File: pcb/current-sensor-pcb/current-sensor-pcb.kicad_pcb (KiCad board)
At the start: 2 copper layers, 35 x 45.2 mm, 17 parts, among them U1 TLI4971A050T5UE0001XUMA1

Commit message: Current sensor progress
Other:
- board size 35 x 45.2 mm -> 35 x 43.5 mm

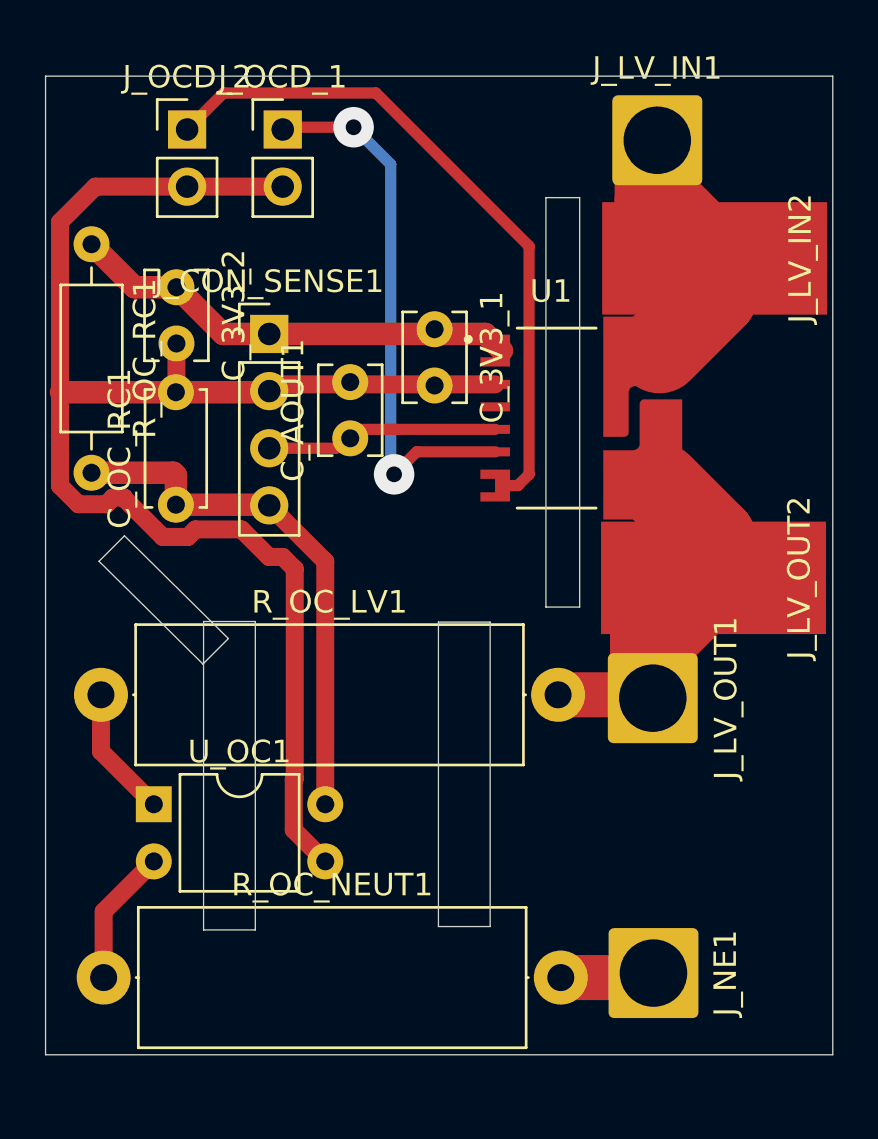
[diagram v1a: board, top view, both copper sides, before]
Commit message: Fixes to relief, JST connectors for SMT board
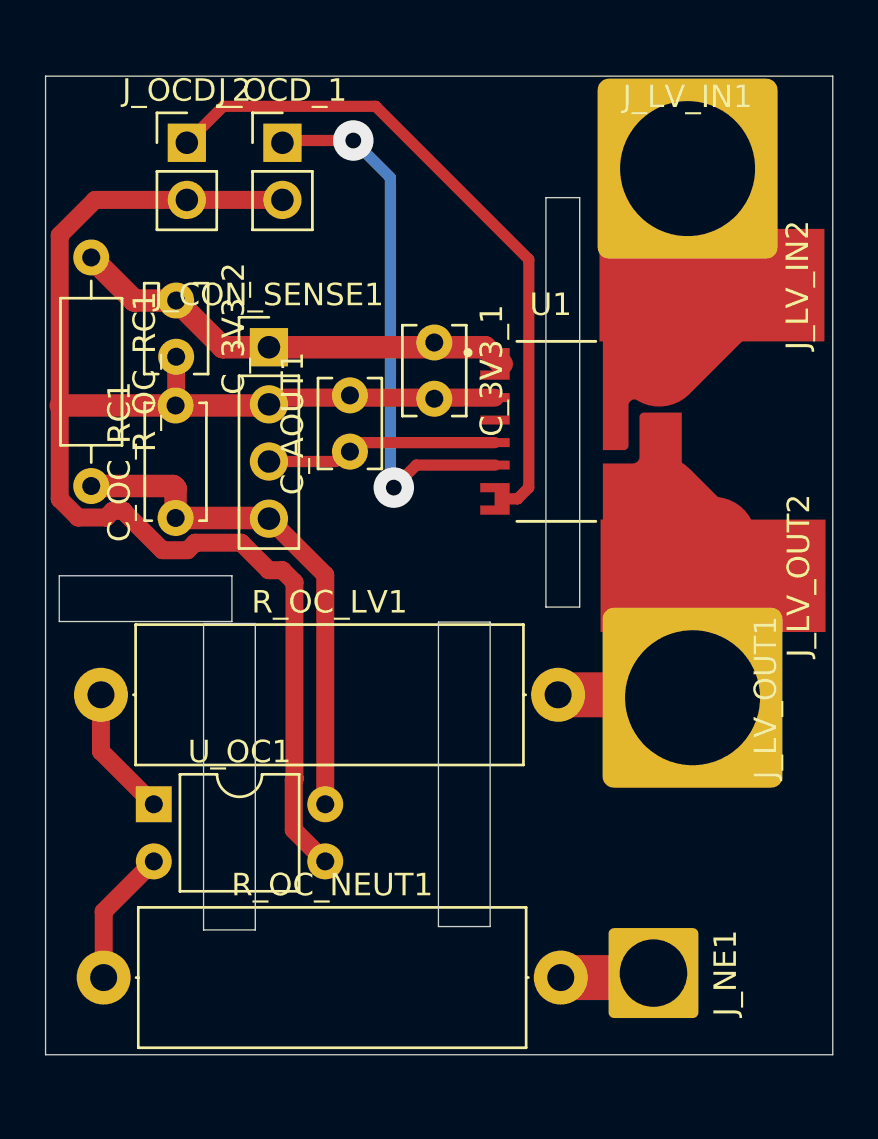
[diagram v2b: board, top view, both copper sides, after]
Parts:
- moved J_LV_IN1 1.84 mm to (28.7, 3.96)
- moved J_LV_OUT1 1.77 mm to (28.9, 27.5)
- moved J_LV_IN2 1.20 mm to (29.7, 9.14)
- moved C_3V3_1 0.59 mm to (17.4, 11.7)
- moved C_3V3_2 0.59 mm to (5.92, 9.82)
- moved C_AOUT1 0.59 mm to (13.6, 16.5)
- moved C_OC_RC1 0.59 mm to (5.89, 19.5)
- moved J_CON_SENSE1 0.59 mm to (10.0, 11.9)
- moved J_OCD_1 0.59 mm to (10.6, 2.81)
- moved J_OCD_2 0.59 mm to (6.39, 2.81)
- moved R_OC_RC1 0.59 mm to (2.14, 7.91)
- moved U1 0.59 mm to (23.9, 15.6)
- moved J_LV_OUT2 0.09 mm to (29.8, 22.1)
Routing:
- net Net-(J_CON_SENSE1-Pin_4): track 23.6 -> 23.0 mm
- net GND: track 70.0 -> 69.4 mm
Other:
- outline, holes or cut-outs redrawn

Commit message: Final changes pre manufacture
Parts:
- added J_NE2: Conn_01x01_Socket, Connector_Wire:SolderWire-2.5sqmm_1x01_D2.4mm_OD3.6mm, F.Cu at (31.2, 39.7)
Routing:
- net Net-(J_NE1-Pin_1): track 4.20 -> 8.24 mm
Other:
- board text added: "current-sensor V1 2025-05-20"
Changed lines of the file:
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@@
 	(footprint "Connector_Wire:SolderWire-2.5sqmm_1x01_D2.4mm_OD3.6mm"
 		(layer "F.Cu")
+		(at 31.1714 39.7166)
+		(descr "Soldered wire connection, for a single 2.5 mm² wire, basic insulation, conductor diameter 2.4mm, outer diameter 3.6mm, size source Multi-Contact FLEXI-E 2.5 (https://ec.staubli.com/AcroFiles/Catalogues/TM_Cab-Main-11014119_(en)_hi.pdf), bend radius 3 times outer diameter, generated with kicad-footprint-generator")
+		(tags "connector wire 2.5sqmm")
+		(property "Reference" "J_NE2"
+			(at 0 -3.2 0)
+			(layer "F.SilkS")
+			(effects
+				(font
+					(size 1 1)
+					(thickness 0.15)
+				)
+			)
+		)
+		(property "Value" "Conn_01x01_Socket"
+			(at 0 3.2 0)
+			(layer "F.Fab")
+			(effects
+				(font
+					(size 1 1)
+					(thickness 0.15)
+				)
+			)
+		)
+		(property "Footprint" "Connector_Wire:SolderWire-2.5sqmm_1x01_D2.4mm_OD3.6mm"
+			(at 0 0 0)
+			(unlocked yes)
+			(layer "F.Fab")
+			(hide yes)
+			(effects
+				(font
+					(size 1.27 1.27)
+					(thickness 0.15)
+				)
+			)
+		)
+		(property "Datasheet" ""
+			(at 0 0 0)
+			(unlocked yes)
+			(layer "F.Fab")
+			(hide yes)
+			(effects
+				(font
+					(size 1.27 1.27)
+					(thickness 0.15)
+				)
+			)
+		)
+		(property "Description" "Generic connector, single row, 01x01, script generated"
+			(at 0 0 0)
+			(unlocked yes)
+			(layer "F.Fab")
+			(hide yes)
+			(effects
+				(font
+					(size 1.27 1.27)
+					(thickness 0.15)
+				)
+			)
+		)
+		(property ki_fp_filters "Connector*:*_1x??_*")
+		(sheetname "Root")
+		(sheetfile "current-sensor-pcb.kicad_sch")
+		(attr exclude_from_pos_files)
+		(fp_line
+			(start -2.55 -2.5)
+			(end -2.55 2.5)
+			(stroke
+				(width 0.05)
+				(type solid)
+			)
+			(layer "F.CrtYd")
+		)
+		(fp_line
+			(start -2.55 2.5)
+			(end 2.55 2.5)
+			(stroke
+				(width 0.05)
+				(type solid)
+			)
+			(layer "F.CrtYd")
+		)
+		(fp_line
+			(start 2.55 -2.5)
+			(end -2.55 -2.5)
+			(stroke
+				(width 0.05)
+				(type solid)
+			)
+			(layer "F.CrtYd")
+		)
+		(fp_line
+			(start 2.55 2.5)
+			(end 2.55 -2.5)
+			(stroke
+				(width 0.05)
+				(type solid)
+			)
+			(layer "F.CrtYd")
+		)
+		(fp_circle
+			(center 0 0)
+			(end 1.8 0)
+			(stroke
+				(width 0.1)
+				(type solid)
+			)
+			(fill none)
+			(layer "F.Fab")
+		)
+		(fp_text user "${REFERENCE}"
+			(at 0 0 0)
+			(layer "F.Fab")
+			(effects
+				(font
+					(size 0.9 0.9)
+					(thickness 0.14)
+				)
+			)
+		)
+		(pad "1" thru_hole roundrect
+			(at 0 0)
+			(size 4 4)
+			(drill 3)
+			(layers "*.Cu" "*.Mask" "In1.Cu" "In2.Cu" "In3.Cu" "In4.Cu" "In5.Cu" "In6.Cu"
+				"In7.Cu" "In8.Cu" "In9.Cu" "In10.Cu" "In11.Cu" "In12.Cu" "In13.Cu" "In14.Cu"
+				"In15.Cu" "In16.Cu" "In17.Cu" "In18.Cu" "In19.Cu" "In20.Cu" "In21.Cu"
+				"In22.Cu" "In23.Cu" "In24.Cu" "In25.Cu" "In26.Cu" "In27.Cu" "In28.Cu"
+				"In29.Cu" "In30.Cu"
+			)
+			(remove_unused_layers no)
+			(roundrect_rratio 0.0625)
+			(net 7 "Net-(J_NE1-Pin_1)")
+			(pinfunction "Pin_1")
+			(pintype "passive")
+		)
+		(model "${KICAD8_3DMODEL_DIR}/Connector_Wire.3dshapes/SolderWire-2.5sqmm_1x01_D2.4mm_OD3.6mm.wrl"
+			(offset
+				(xyz 0 0 0)
+			)
+			(scale
+				(xyz 1 1 1)
+			)
+			(rotate
+				(xyz 0 0 0)
+			)
+		)
+	)
+	(footprint "Connector_Wire:SolderWire-2.5sqmm_1x01_D2.4mm_OD3.6mm"
+		(layer "F.Cu")
 		(at 27.1344 39.7166 -90)
 		(descr "Soldered wire connection, for a single 2.5 mm² wire, basic insulation, conductor diameter 2.4mm, outer diameter 3.6mm, size source Multi-Contact FLEXI-E 2.5 (https://ec.staubli.com/AcroFiles/Catalogues/TM_Cab-Main-11014119_(en)_hi.pdf), bend radius 3 times outer diameter, generated with kicad-footprint-generator")
@@
 		)
 		(property "Value" "Conn_01x01_Socket"
-			(at 0 6.35 90)
+			(at -3.44 -4.08 90)
 			(layer "F.Fab")
 			(effects
@@
 		)
 		(property "Value" "TLI4971A050T5UE0001XUMA1"
-			(at 12.645 5.635 0)
+			(at -6.28 -0.33 -90)
 			(layer "F.Fab")
 			(effects
@@
 		)
 		(property "Value" "Conn_01x01_Socket"
-			(at 0 6.35 90)
+			(at 5.52 -3.93 90)
 			(layer "F.Fab")
 			(effects
@@
 		(layer "Edge.Cuts")
 	)
+	(gr_text "current-sensor\nV1 2025-05-20"
+		(at 21.1814 35.1966 0)
+		(layer "F.SilkS")
+		(effects
+			(font
+				(size 1 1)
+				(thickness 0.15)
+			)
+			(justify left bottom)
+		)
+	)
 	(segment
 		(start 3.0986 19.1666)
@@
 		(width 2)
 		(layer "F.Cu")
+		(net 7)
+	)
+	(segment
+		(start 27.1344 39.7166)
+		(end 31.1714 39.7166)
+		(width 2)
+		(layer "F.Cu")
